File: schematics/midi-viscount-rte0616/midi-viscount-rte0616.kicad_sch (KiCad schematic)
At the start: 8 parts, among them J1 Conn_02x07_Odd_Even, U1 ProMicro

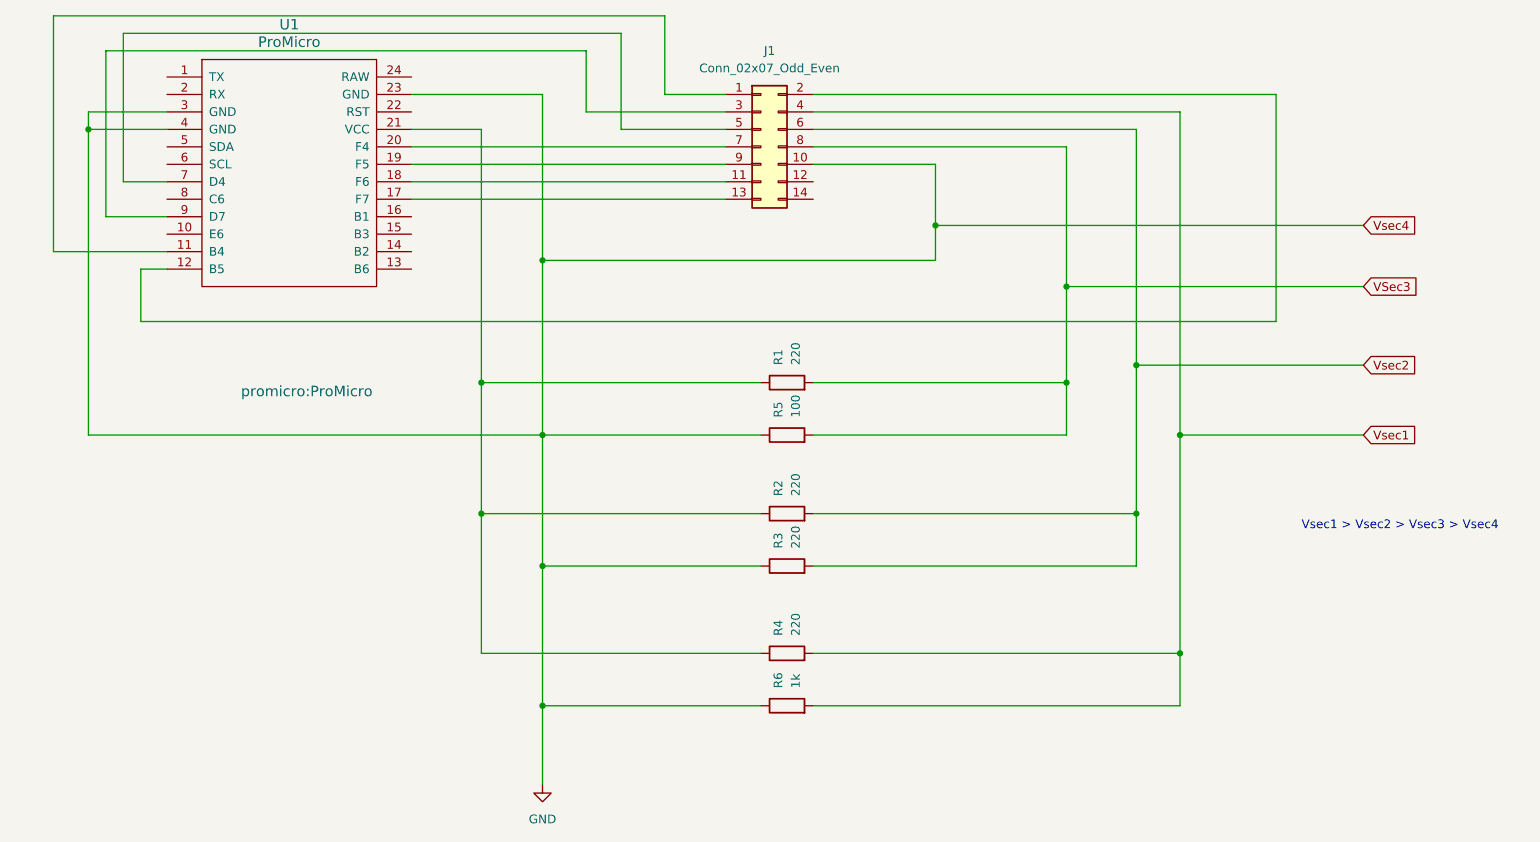
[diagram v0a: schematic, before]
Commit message: Use potentiometers instead of resistors
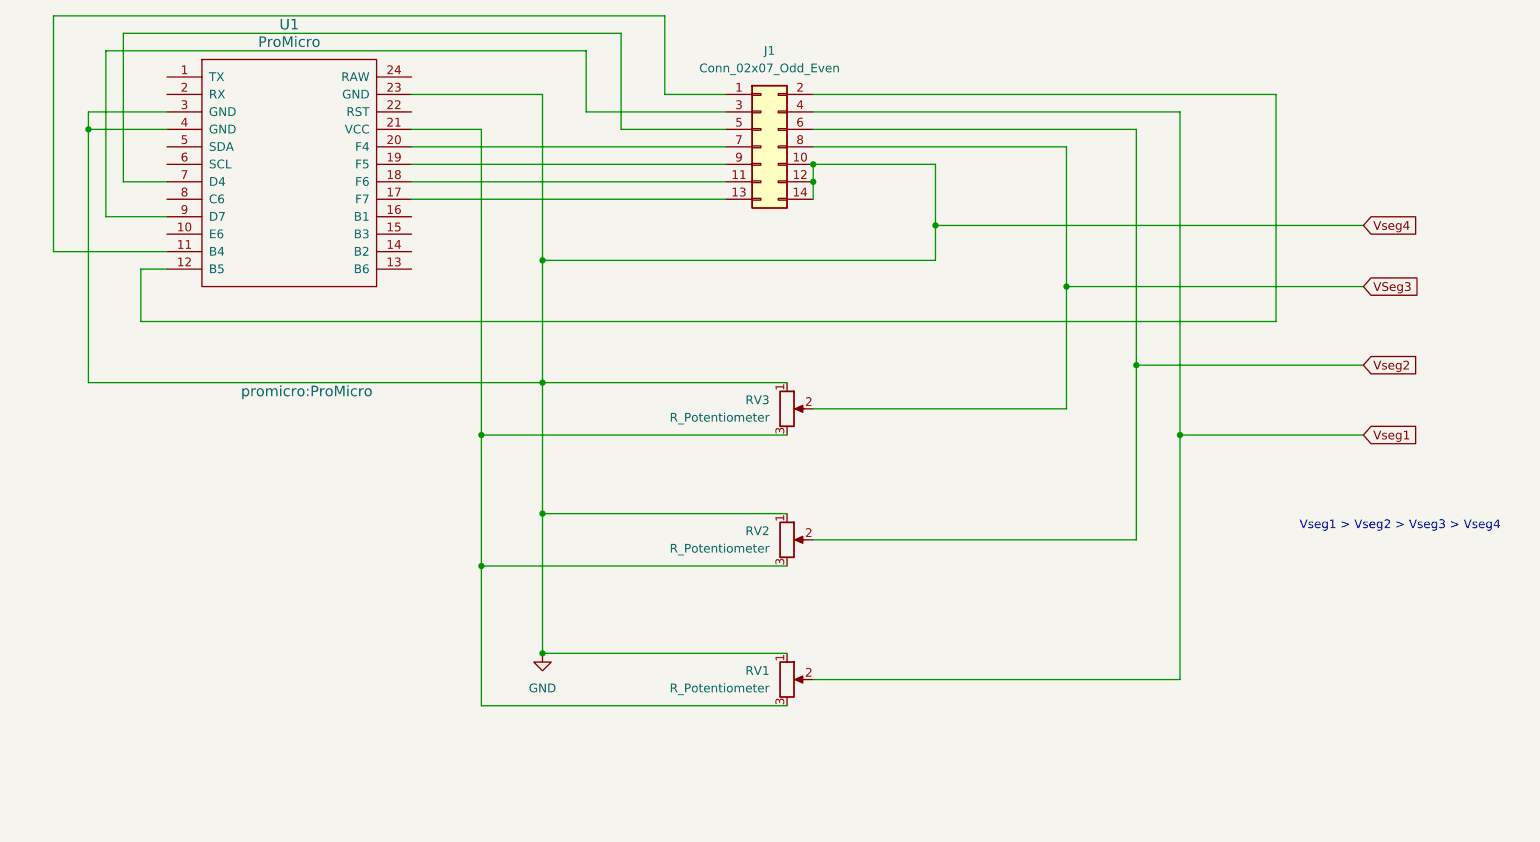
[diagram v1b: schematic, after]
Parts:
- removed R1, R2, R3, R4: 220, Resistor_THT:R_Axial_DIN0204_L3.6mm_D1.6mm_P7.62mm_Horizontal, symbol Device:R
- removed R5: 100, Resistor_THT:R_Axial_DIN0204_L3.6mm_D1.6mm_P7.62mm_Horizontal, symbol Device:R
- removed R6: 1k, Resistor_THT:R_Axial_DIN0204_L3.6mm_D1.6mm_P7.62mm_Horizontal, symbol Device:R
- added RV1, RV2, RV3: R_Potentiometer, Potentiometer_THT:Potentiometer_Bourns_3266Y_Vertical, symbol Device:R_Potentiometer
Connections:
- net GND: now also J1.12 (Pin_12), J1.14 (Pin_14), RV1.1, RV2.1, RV3.1
- net at U1.21 (VCC): now also RV1.3, RV2.3, RV3.3
- net VSec3 renamed VSeg3
- net VSeg3: now also RV3.2
- net Vsec1 renamed Vseg1
- net Vseg1: now also RV1.2
- net Vsec2 renamed Vseg2
- net Vseg2: now also RV2.2
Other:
- note added: "Vseg1 > Vseg2 > Vseg3 > Vseg4"
- note removed: "Vsec1 > Vsec2 > Vsec3 > Vsec4"

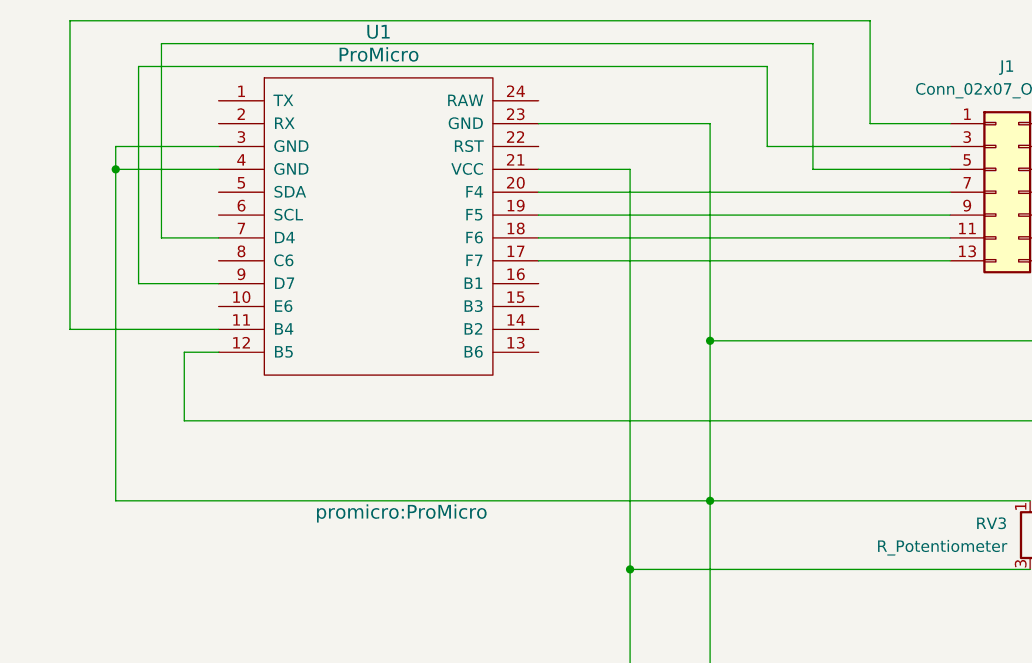
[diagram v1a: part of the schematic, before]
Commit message: Add pin headers for pedals
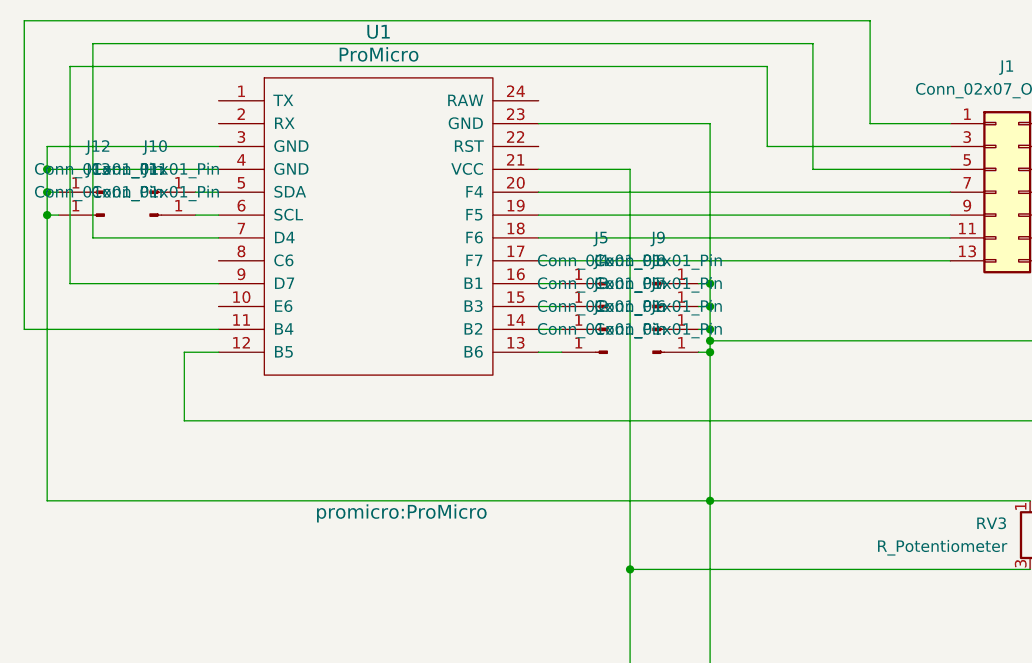
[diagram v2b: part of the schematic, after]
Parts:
- added J10, J11, J12, J13, J2, J3, J4, J5, J6, J7, J8, J9: Conn_01x01_Pin, Connector_PinHeader_2.54mm:PinHeader_1x01_P2.54mm_Vertical, symbol Connector:Conn_01x01_Pin
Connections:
- net GND: now also J12.1 (Pin_1), J13.1 (Pin_1), J6.1 (Pin_1), J7.1 (Pin_1), J8.1 (Pin_1), J9.1 (Pin_1)
- net at U1.13 (B6): now also J2.1 (Pin_1)
- net at U1.14 (B2): now also J3.1 (Pin_1)
- net at U1.15 (B3): now also J4.1 (Pin_1)
- net at U1.16 (B1): now also J5.1 (Pin_1)
- net at U1.5 (SDA): now also J10.1 (Pin_1)
- net at U1.6 (SCL): now also J11.1 (Pin_1)

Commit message: Schematics rev1.1
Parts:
- renumbered J12 to J11, J11 to J12, J6 to J3, J3 to J4, J7 to J5, J4 to J6, J8 to J7, J5 to J8
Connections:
- net GND: now also J1.1 (Pin_1), J1.3 (Pin_3), J1.5 (Pin_5); no longer J1.10 (Pin_10), J1.12 (Pin_12), J1.14 (Pin_14)
- net VSeg3: now also J1.7 (Pin_7); no longer J1.8 (Pin_8)
- net Vseg1: now also J1.11 (Pin_11); no longer J1.4 (Pin_4)
- net Vseg2: now also J1.9 (Pin_9); no longer J1.6 (Pin_6)
- net at U1.11 (B4): now also J1.14 (Pin_14); no longer J1.1 (Pin_1)
- net at U1.12 (B5): now also J1.13 (Pin_13); no longer J1.2 (Pin_2)
- net at U1.17 (F7): now also J1.2 (Pin_2); no longer J1.13 (Pin_13)
- net at U1.18 (F6): now also J1.4 (Pin_4); no longer J1.11 (Pin_11)
- net at U1.19 (F5): now also J1.6 (Pin_6); no longer J1.9 (Pin_9)
- net at U1.20 (F4): now also J1.8 (Pin_8); no longer J1.7 (Pin_7)
- net at U1.7 (D4): now also J1.10 (Pin_10); no longer J1.5 (Pin_5)
- net at U1.9 (D7): now also J1.12 (Pin_12); no longer J1.3 (Pin_3)
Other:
- moved on the sheet: J1
